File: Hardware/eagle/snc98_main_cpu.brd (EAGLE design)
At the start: 168.2 x 30 mm, 89 parts, among them IC1 MCP170333MB, M1 IRLML2244, M12 IRLML2244, M2 IRLML2244, M3 IRLML2244, T1 BCR135, T2 BCR135, T3 BCR185, U1 74HC4051_MUX, U2 DS18B20, U3 ATMEGA1284P-PU, U4 TLV70033 / TC1185, Y2 12MHz

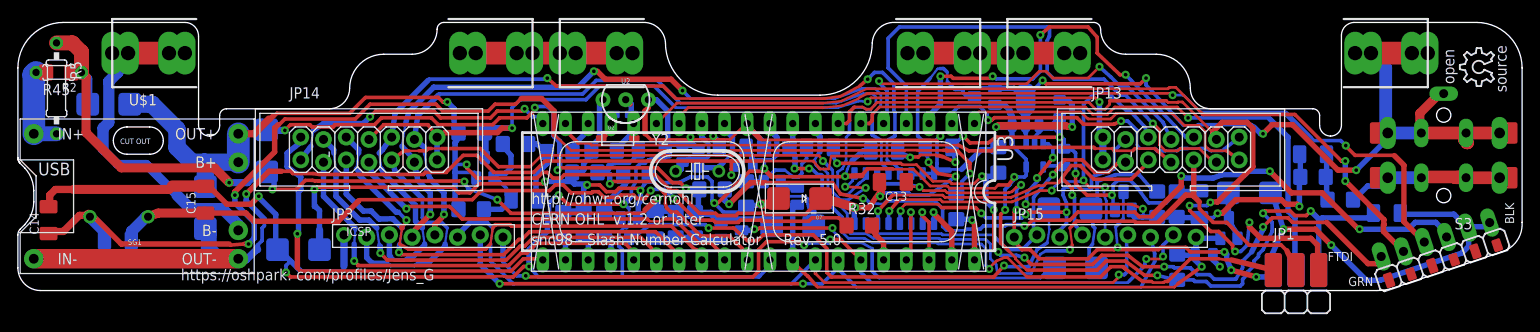
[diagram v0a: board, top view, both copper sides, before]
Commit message: PCB cleaning V1.1
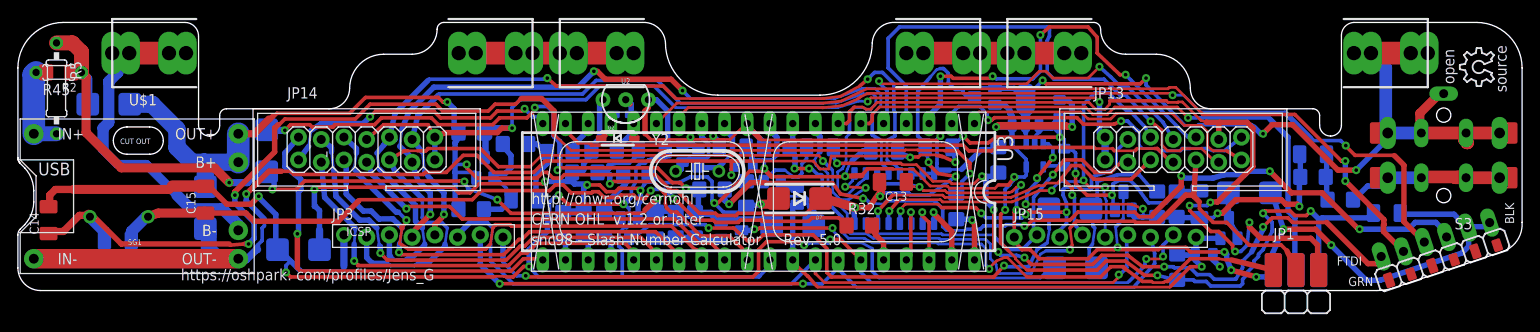
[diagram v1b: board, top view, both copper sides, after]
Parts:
- moved JP13 0.25 mm to (122.6, 12.7)
- moved JP14 0.25 mm to (32.4, 12.7)
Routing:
- net B_MINUS: track 39.4 -> 65.7 mm
- net P3: track 19.3 -> 28.3 mm
- net P2: track 19.3 -> 26.7 mm
- net N$6: track 24.0 -> 21.2 mm
- net V_IN: track 263.9 -> 262.2 mm
- net AREF_+1V: track 63.6 -> 65.1 mm
- net N$13: track 11.8 -> 10.6 mm
- net D6_: track 90.2 -> 89.2 mm
- net D15_: track 45.1 -> 44.4 mm
- net IO_F: track 82.9 -> 83.5 mm

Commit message: sinh()_cosh()_tanh() added
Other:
- board text added: "snc98 - Slash Number Calculator Rev. 1.1"
- board text removed: "snc98 - Slash Number Calculator Rev. 5.0"

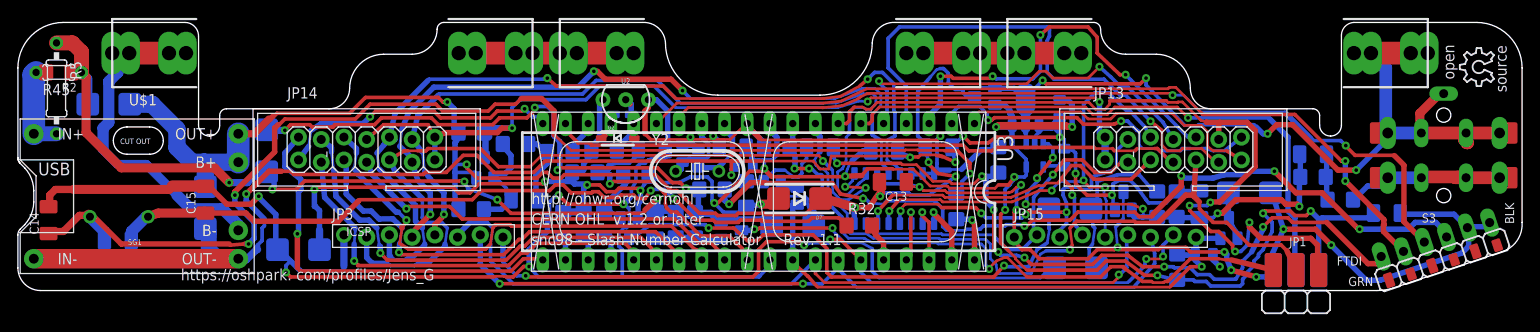
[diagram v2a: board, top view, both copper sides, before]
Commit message: PCB - add Tear Drop
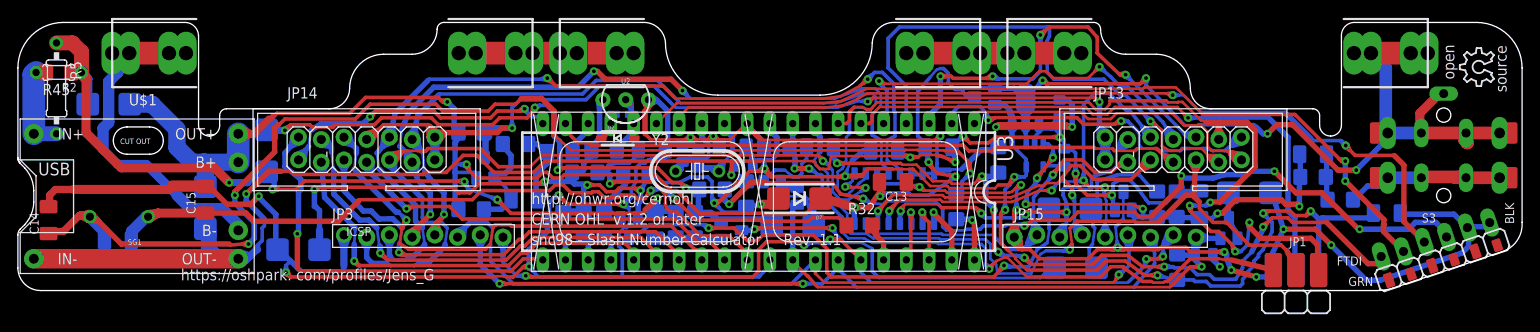
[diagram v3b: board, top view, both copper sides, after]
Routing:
- net GND-ISO: track 328.9 -> 392.8 mm
- net VCC: track 253.2 -> 298.6 mm
- net CA_PWM: track 111.0 -> 145.9 mm
- net GND: track 182.9 -> 214.0 mm
- net V_IN: track 262.2 -> 289.6 mm
- net A5: track 88.4 -> 113.6 mm
- net IO_A: track 52.7 -> 76.5 mm
- net IO_C: track 39.3 -> 62.2 mm
- net IO_DP: track 89.1 -> 110.6 mm
- net DTR: track 82.1 -> 102.4 mm
- net D2_: track 46.4 -> 64.5 mm
- net IO_G: track 96.6 -> 114.4 mm
- net EN: track 49.9 -> 66.6 mm
- net VIN_P: track 92.6 -> 106.6 mm
- net D6_: track 89.6 -> 103.5 mm
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
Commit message: Gerber file added
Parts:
- added C17, C19: 1µ, rcl:C1206K
- added C23: 220n, SparkFun:0805
- C20, C21: value 4.7uF -> 1uF
- C7, C8: value 15pF -> 22pF
- R25: value 100 -> 47
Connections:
- net DTR: now also C23.4
- net GND: now also C17.2, C19.2
- net R_: now also C23.3
- net VCC: now also C17.1
- net V_IN: now also C19.1
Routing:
- net GND: track 214.0 -> 215.9 mm
- net DTR: track 102.4 -> 103.0 mm
- net R_: track 10.3 -> 10.8 mm

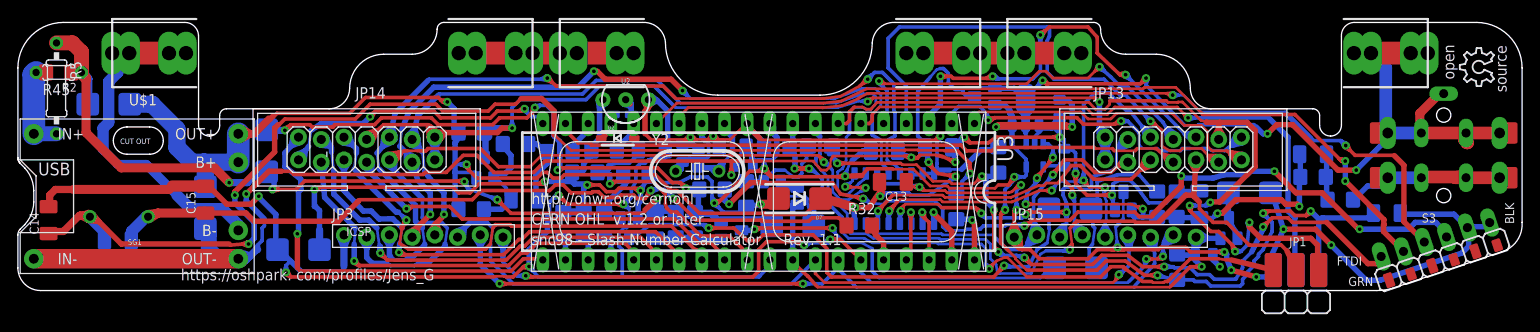
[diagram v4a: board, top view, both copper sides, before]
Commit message: more accurate Factorial Function n!
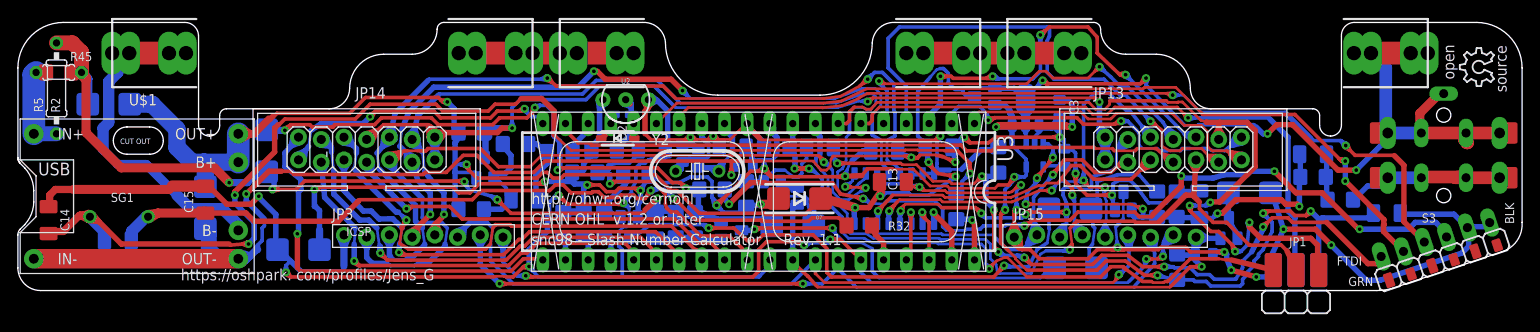
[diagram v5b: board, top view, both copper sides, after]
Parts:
- removed C20, C21: 1uF, SparkFun:EIA3216
- removed C23: 220n, SparkFun:0805
- R4: value 100 -> 47
- moved M2 0.13 mm to (61.7, 4.06)
- renumbered R44 to 44, R46 to 46, R47 to 47, U$2 to M4
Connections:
- net DTR: no longer C23.4
- net GND: no longer C20.C, C21.C
- net R_: no longer C23.3
- net VCC: no longer C20.A
- net V_IN: no longer C21.A
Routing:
- net VCC: track 299.0 -> 300.3 mm
- net GND-ISO: track 392.8 -> 392.2 mm, vias 18 -> 17
- net R_: track 10.8 -> 10.3 mm

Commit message: change_to_6mm_taktile_switch
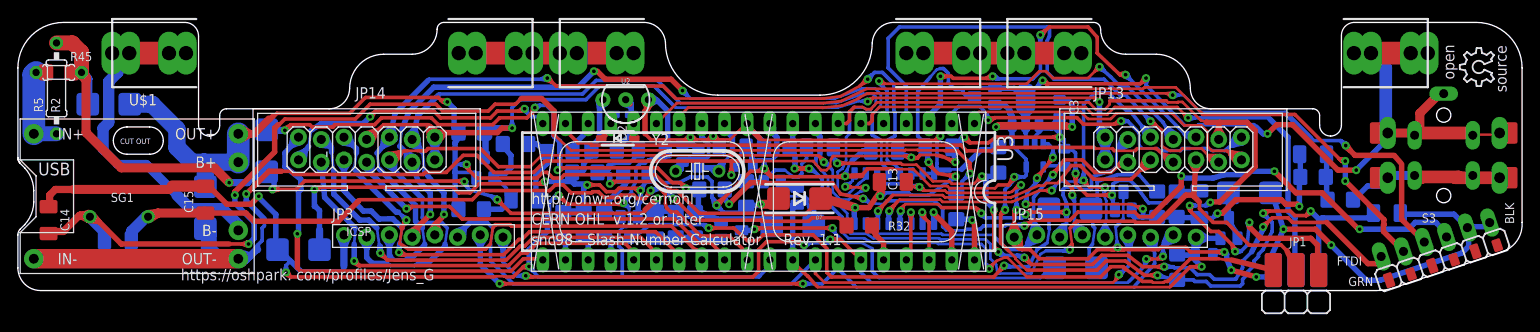
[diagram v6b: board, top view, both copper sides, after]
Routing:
- net N$6: track 21.2 -> 23.3 mm
- net V_IN: track 289.6 -> 287.8 mm

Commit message: cleanup_PCB
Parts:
- C3: value 220nF -> 1µ; device SparkFun:0805 -> rcl:C1206K
- moved JP6 5.07 mm to (147.7, -3.94)
- moved C2 0.65 mm to (146.3, 4.98)
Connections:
- net D8_RX0: now also JP6.P4, JP6.P4A; no longer JP6.3
- net D9_TX0: now also JP6.P5, JP6.P5A; no longer JP6.2
- net DTR: now also JP6.P6, JP6.P6A; no longer JP6.1
- net GND: now also C3.2; no longer C3.4
- net GND-ISO: now also JP6.P1, JP6.P1A, JP6.P2, JP6.P2A; no longer JP6.5, JP6.6
- net VCC: now also C3.1; no longer C3.3
- net VCC_IN: now also JP6.P3, JP6.P3A; no longer JP6.4
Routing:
- net CA_PWM: track 145.9 -> 891.1 mm
- net GND-ISO: track 392.2 -> 1017.8 mm, vias 17 -> 19
- net VCC: track 300.3 -> 855.5 mm
- net GND: track 215.9 -> 596.9 mm
- net DTR: track 103.3 -> 369.1 mm, vias 7 -> 9
- net V_IN: track 287.8 -> 528.4 mm
- net IO_DP: track 111.0 -> 350.0 mm
- net IO_A: track 76.5 -> 314.5 mm
- net A5: track 113.6 -> 341.5 mm
- net IO_C: track 62.2 -> 284.3 mm
- net IO_G: track 114.4 -> 295.9 mm
- net EN: track 66.6 -> 226.7 mm
- net D2_: track 64.5 -> 208.9 mm
- net D6_: track 103.5 -> 246.0 mm
- net IO_B: track 57.0 -> 194.9 mm
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
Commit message: cbrt_int96
cbrt added
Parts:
- D10, D11, D12, D3, D4, D5, D7, D8, D9: device BaseApp:SMADIODE -> BaseApp:SOD-123F
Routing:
- net IO_C: track 284.3 -> 197.1 mm
- net VCC: track 855.5 -> 858.7 mm
- net VIN_P: track 183.5 -> 185.8 mm
- net GND-ISO: track 1017.8 -> 1019.8 mm
- net V_IN: track 528.4 -> 530.0 mm
- net CA_PWM2: track 95.2 -> 93.6 mm
- net IO_B: track 194.9 -> 196.4 mm
- net GND_POWER: track 5.48 -> 6.30 mm
- net GND: track 596.9 -> 597.7 mm
- net EN_: track 18.4 -> 19.1 mm
- net XX_3: track 163.6 -> 163.0 mm
